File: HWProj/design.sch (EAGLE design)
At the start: 72 parts, among them IC1 LM311N, IC10 TL071P, IC11 TL071P, IC12 TL071P, IC13 TL071P, IC14 TL071P, IC15 TL071P, IC16 LM311N, IC17 TL071P, IC18 TL071P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

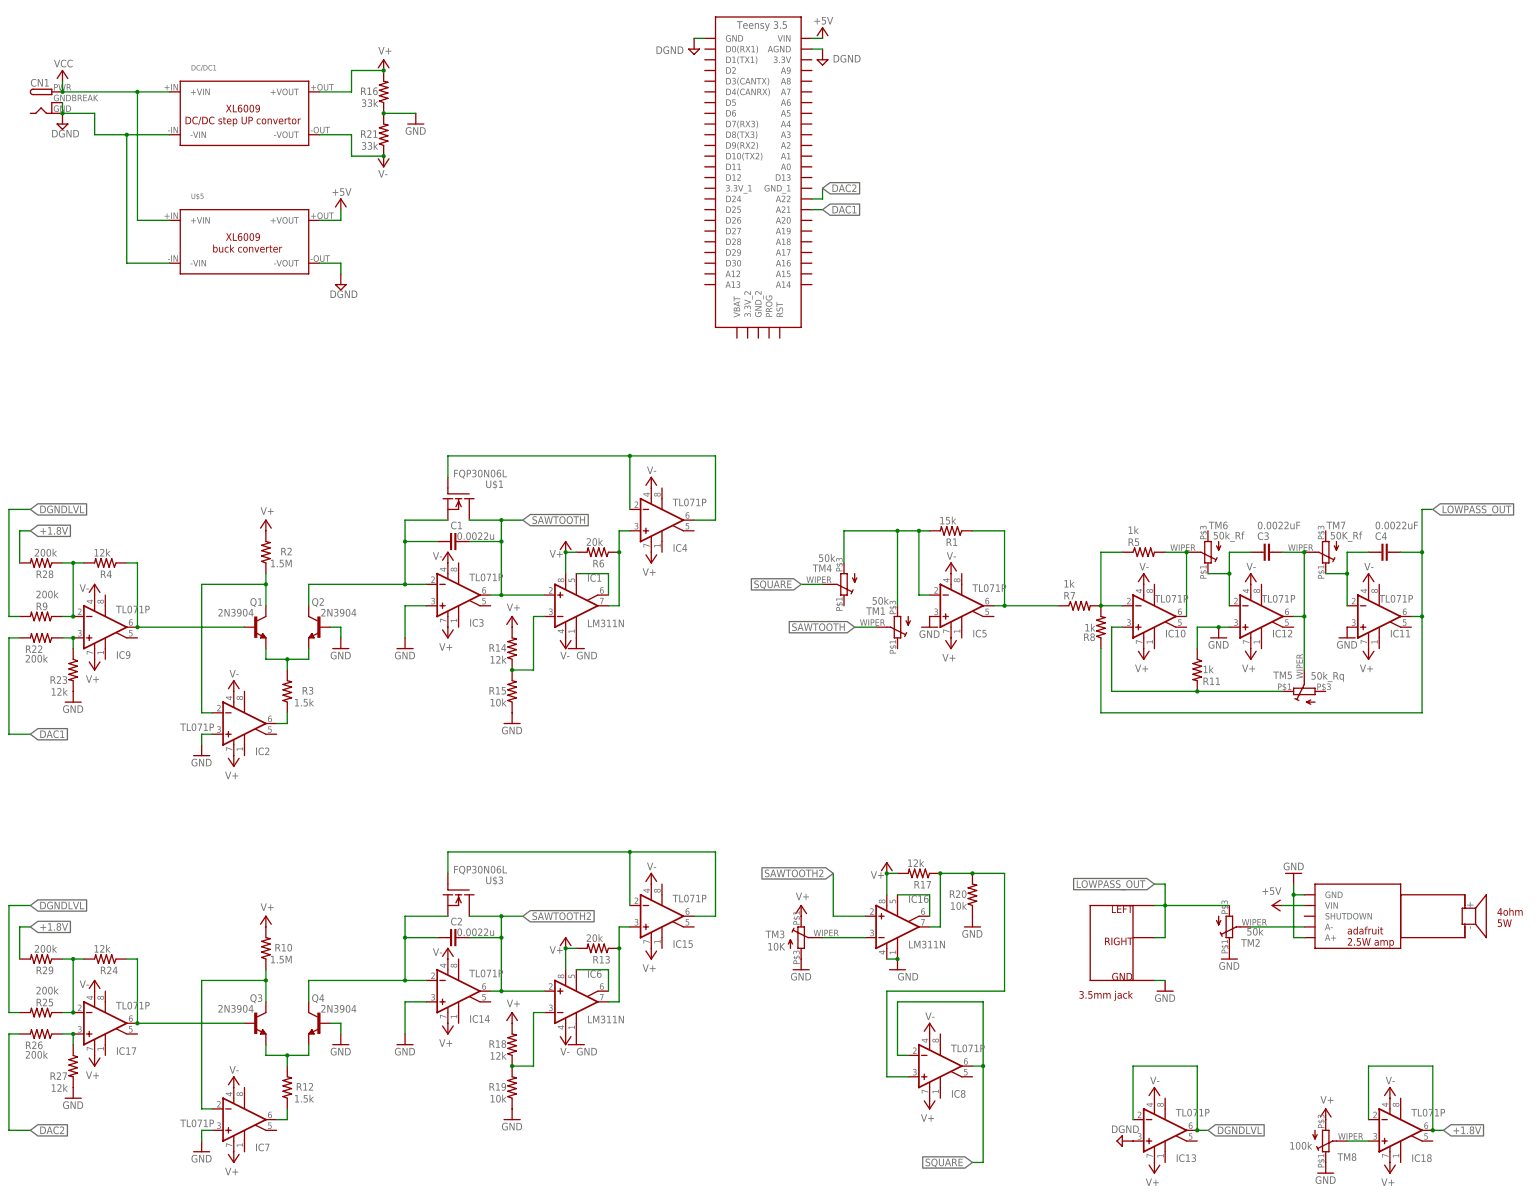
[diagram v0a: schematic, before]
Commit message: fixed ground ref for amp, replaced boost converter
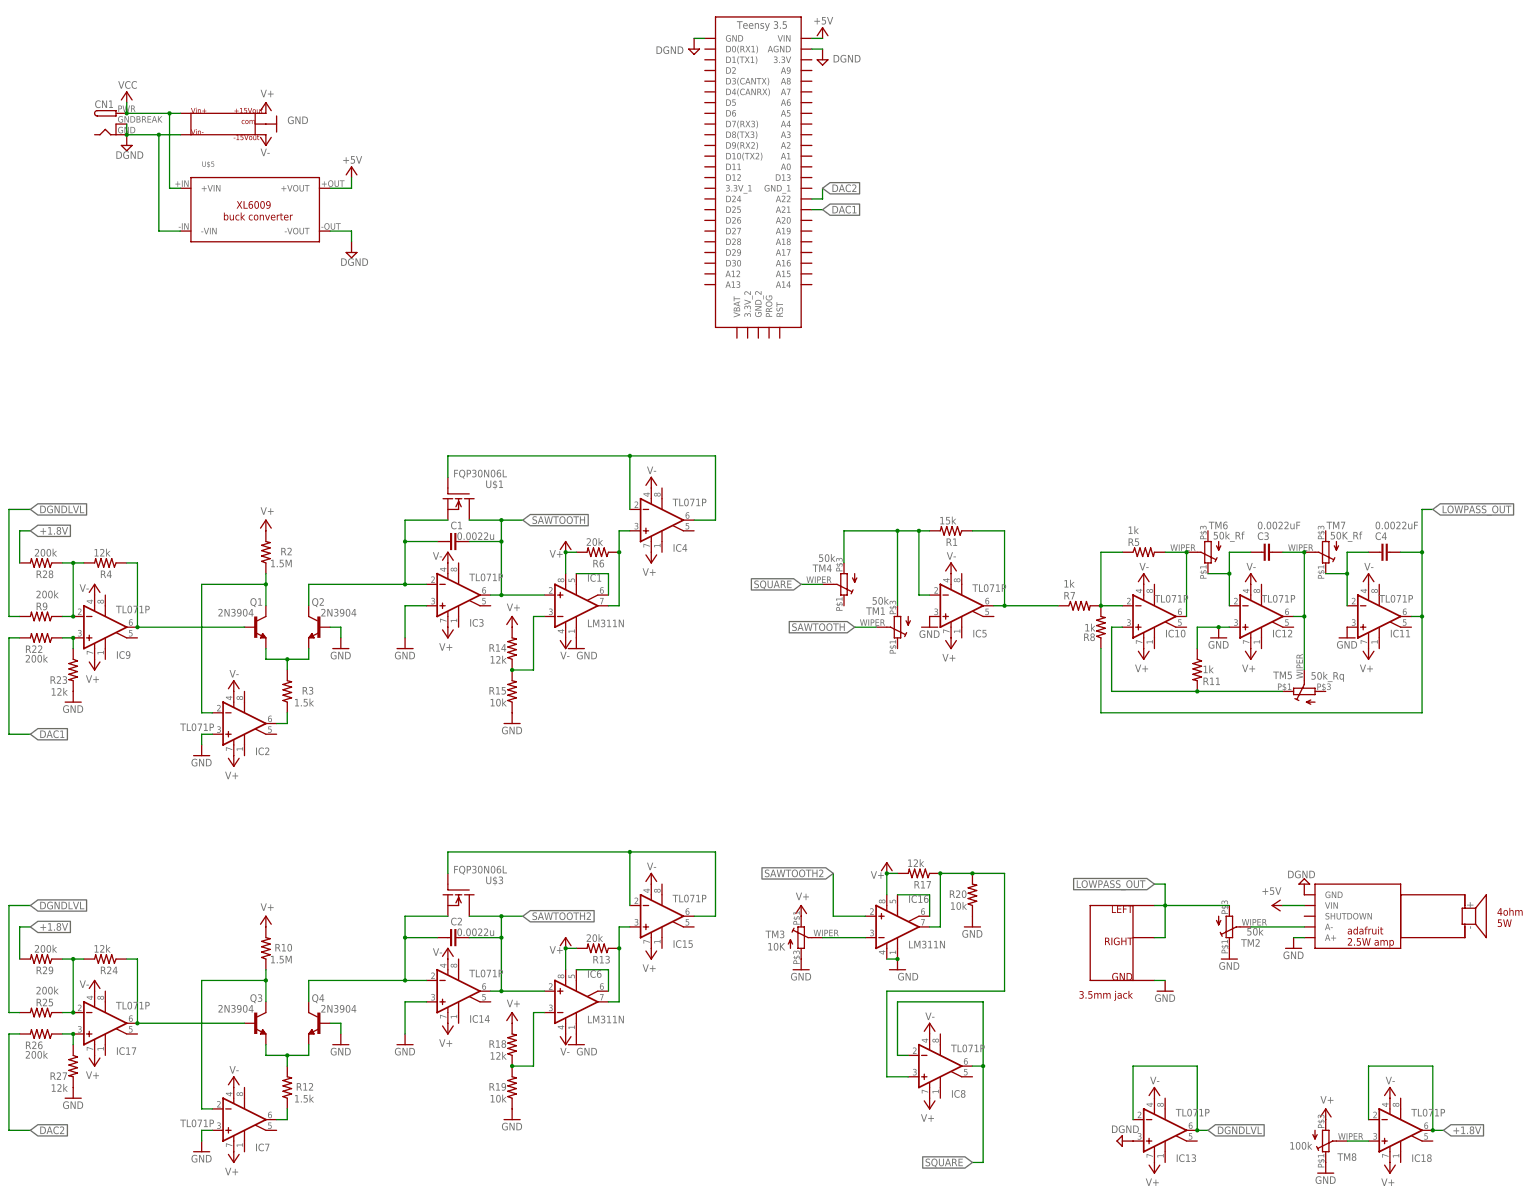
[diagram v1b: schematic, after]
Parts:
- removed DC/DC1: DC/DC-STEP-UP-XL6009, userlib:DC/DC-STEP-UP-XL6009
- removed R16, R21: 33k, HyTechDevices:RESISTORAXIAL-0.3
- added U$7: +/-15V_BOOST_CONVERTER, userlib:+/-15V_BOOST_CONVERTER
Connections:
- net DGND: now also U$2.GND, U$7.1; no longer DC/DC1.-VIN
- net GND: now also U$7.7; no longer R16.1, R21.2, U$2.GND
- net V+: now also U$7.6; no longer DC/DC1.+VOUT, R16.2
- net V-: now also U$7.8; no longer DC/DC1.-VOUT, R21.1
- net VCC: now also U$7.2; no longer DC/DC1.+VIN
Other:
- note added: "needs testing!!"
- note removed: "+/-15V"
- moved on the sheet: CN1, U$5

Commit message: added board rev0
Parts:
- C1, C2: device HyTechDevices:CAPCAP_WIMA -> HyTechDevices:CAPPTH1
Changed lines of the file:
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@@
 <layers>
 <layer number="1" name="Top" color="4" fill="1" visible="yes" active="no"/>
-<layer number="2" name="Route2" color="1" fill="3" visible="yes" active="no"/>
-<layer number="3" name="Route3" color="4" fill="3" visible="yes" active="no"/>
-<layer number="4" name="Route4" color="1" fill="4" visible="yes" active="no"/>
-<layer number="5" name="Route5" color="4" fill="4" visible="yes" active="no"/>
-<layer number="6" name="Route6" color="1" fill="8" visible="yes" active="no"/>
-<layer number="7" name="Route7" color="4" fill="8" visible="yes" active="no"/>
-<layer number="8" name="Route8" color="1" fill="2" visible="yes" active="no"/>
-<layer number="9" name="Route9" color="4" fill="2" visible="yes" active="no"/>
-<layer number="10" name="Route10" color="1" fill="7" visible="yes" active="no"/>
-<layer number="11" name="Route11" color="4" fill="7" visible="yes" active="no"/>
-<layer number="12" name="Route12" color="1" fill="5" visible="yes" active="no"/>
-<layer number="13" name="Route13" color="4" fill="5" visible="yes" active="no"/>
-<layer number="14" name="Route14" color="1" fill="6" visible="yes" active="no"/>
-<layer number="15" name="Route15" color="4" fill="6" visible="yes" active="no"/>
+<layer number="2" name="Route2" color="16" fill="1" visible="yes" active="no"/>
+<layer number="3" name="Route3" color="17" fill="1" visible="yes" active="no"/>
+<layer number="4" name="Route4" color="18" fill="1" visible="yes" active="no"/>
+<layer number="5" name="Route5" color="19" fill="1" visible="yes" active="no"/>
+<layer number="6" name="Route6" color="25" fill="1" visible="yes" active="no"/>
+<layer number="7" name="Route7" color="26" fill="1" visible="yes" active="no"/>
+<layer number="8" name="Route8" color="27" fill="1" visible="yes" active="no"/>
+<layer number="9" name="Route9" color="28" fill="1" visible="yes" active="no"/>
+<layer number="10" name="Route10" color="29" fill="1" visible="yes" active="no"/>
+<layer number="11" name="Route11" color="30" fill="1" visible="yes" active="no"/>
+<layer number="12" name="Route12" color="20" fill="1" visible="yes" active="no"/>
+<layer number="13" name="Route13" color="21" fill="1" visible="yes" active="no"/>
+<layer number="14" name="Route14" color="22" fill="1" visible="yes" active="no"/>
+<layer number="15" name="Route15" color="23" fill="1" visible="yes" active="no"/>
 <layer number="16" name="Bottom" color="1" fill="1" visible="yes" active="no"/>
 <layer number="17" name="Pads" color="2" fill="1" visible="yes" active="no"/>
 <layer number="18" name="Vias" color="2" fill="1" visible="yes" active="no"/>
 <layer number="19" name="Unrouted" color="6" fill="1" visible="yes" active="no"/>
-<layer number="20" name="Dimension" color="15" fill="1" visible="yes" active="no"/>
+<layer number="20" name="Dimension" color="24" fill="1" visible="yes" active="no"/>
 <layer number="21" name="tPlace" color="7" fill="1" visible="yes" active="no"/>
 <layer number="22" name="bPlace" color="7" fill="1" visible="yes" active="no"/>
@@
 <part name="SUPPLY2" library="supply2" library_urn="urn:adsk.eagle:library:372" deviceset="V+" device=""/>
 <part name="GND3" library="HyTechSymbols" deviceset="GND" device=""/>
-<part name="C1" library="HyTechDevices" deviceset="CAP" device="CAP_WIMA" value="0.0022u"/>
+<part name="C1" library="HyTechDevices" deviceset="CAP" device="PTH1" value="0.0022u"/>
 <part name="GND4" library="HyTechSymbols" deviceset="GND" device=""/>
 <part name="SUPPLY3" library="supply2" library_urn="urn:adsk.eagle:library:372" deviceset="V-" device=""/>
@@
 <part name="SUPPLY15" library="supply2" library_urn="urn:adsk.eagle:library:372" deviceset="V+" device=""/>
 <part name="GND11" library="HyTechSymbols" deviceset="GND" device=""/>
-<part name="C2" library="HyTechDevices" deviceset="CAP" device="CAP_WIMA" value="0.0022u"/>
+<part name="C2" library="HyTechDevices" deviceset="CAP" device="PTH1" value="0.0022u"/>
 <part name="GND14" library="HyTechSymbols" deviceset="GND" device=""/>
 <part name="SUPPLY29" library="supply2" library_urn="urn:adsk.eagle:library:372" deviceset="V-" device=""/>
@@
 <part name="U$6" library="userlib" deviceset="3.5MM_AUDIO_JACK" device=""/>
 <part name="SUPPLY39" library="supply2" library_urn="urn:adsk.eagle:library:372" deviceset="DGND" device=""/>
-<part name="U$7" library="userlib" deviceset="+/-15V_BOOST_CONVERTER" device=""/>
 <part name="SUPPLY40" library="supply2" library_urn="urn:adsk.eagle:library:372" deviceset="V+" device=""/>
 <part name="SUPPLY49" library="supply2" library_urn="urn:adsk.eagle:library:372" deviceset="V-" device=""/>
 <part name="GND5" library="HyTechSymbols" deviceset="GND" device=""/>
+<part name="U$7" library="userlib" deviceset="+/-15V_BOOST_CONVERTER" device=""/>
 </parts>
 <sheets>
@@
 <attribute name="VALUE" x="325.247" y="86.995" size="1.778" layer="96" rot="R180"/>
 </instance>
-<instance part="U$7" gate="G$1" x="66.04" y="264.16" smashed="yes"/>
 <instance part="SUPPLY40" gate="1" x="76.2" y="269.24" smashed="yes">
 <attribute name="VALUE" x="74.93" y="270.51" size="1.778" layer="96"/>
@@
 <attribute name="VALUE" x="81.28" y="264.16" size="1.778" layer="96"/>
 </instance>
+<instance part="U$7" gate="G$1" x="66.04" y="264.16" smashed="yes"/>
 </instances>
 <busses>
@@
 </segment>
 <segment>
+<pinref part="SUPPLY40" gate="1" pin="V+"/>
 <pinref part="U$7" gate="G$1" pin="6"/>
-<pinref part="SUPPLY40" gate="1" pin="V+"/>
 </segment>
 </net>
@@
 </segment>
 <segment>
+<pinref part="GND5" gate="1" pin="GND"/>
 <pinref part="U$7" gate="G$1" pin="7"/>
-<pinref part="GND5" gate="1" pin="GND"/>
 </segment>
 </net>
@@
 </segment>
 <segment>
+<pinref part="SUPPLY49" gate="1" pin="V-"/>
 <pinref part="U$7" gate="G$1" pin="8"/>
-<pinref part="SUPPLY49" gate="1" pin="V-"/>
 </segment>
 </net>
@@
 <wire x1="43.18" y1="264.16" x2="43.18" y2="261.62" width="0.1524" layer="91"/>
 <junction x="43.18" y="261.62"/>
-<pinref part="U$7" gate="G$1" pin="1"/>
 <wire x1="43.18" y1="261.62" x2="50.8" y2="261.62" width="0.1524" layer="91"/>
 <pinref part="U$5" gate="G$1" pin="-VIN"/>
@@
 <wire x1="50.8" y1="238.76" x2="50.8" y2="261.62" width="0.1524" layer="91"/>
 <junction x="50.8" y="261.62"/>
+<pinref part="U$7" gate="G$1" pin="1"/>
 </segment>
 <segment>
@@
 <junction x="43.18" y="266.7"/>
 <wire x1="55.88" y1="266.7" x2="53.34" y2="266.7" width="0.1524" layer="91"/>
-<pinref part="U$7" gate="G$1" pin="2"/>
 <pinref part="U$5" gate="G$1" pin="+VIN"/>
 <wire x1="53.34" y1="266.7" x2="43.18" y2="266.7" width="0.1524" layer="91"/>
@@
 <wire x1="53.34" y1="248.92" x2="53.34" y2="266.7" width="0.1524" layer="91"/>
 <junction x="53.34" y="266.7"/>
-</segment>
-</net>
+<pinref part="U$7" gate="G$1" pin="2"/>
+</segment>
+</net>

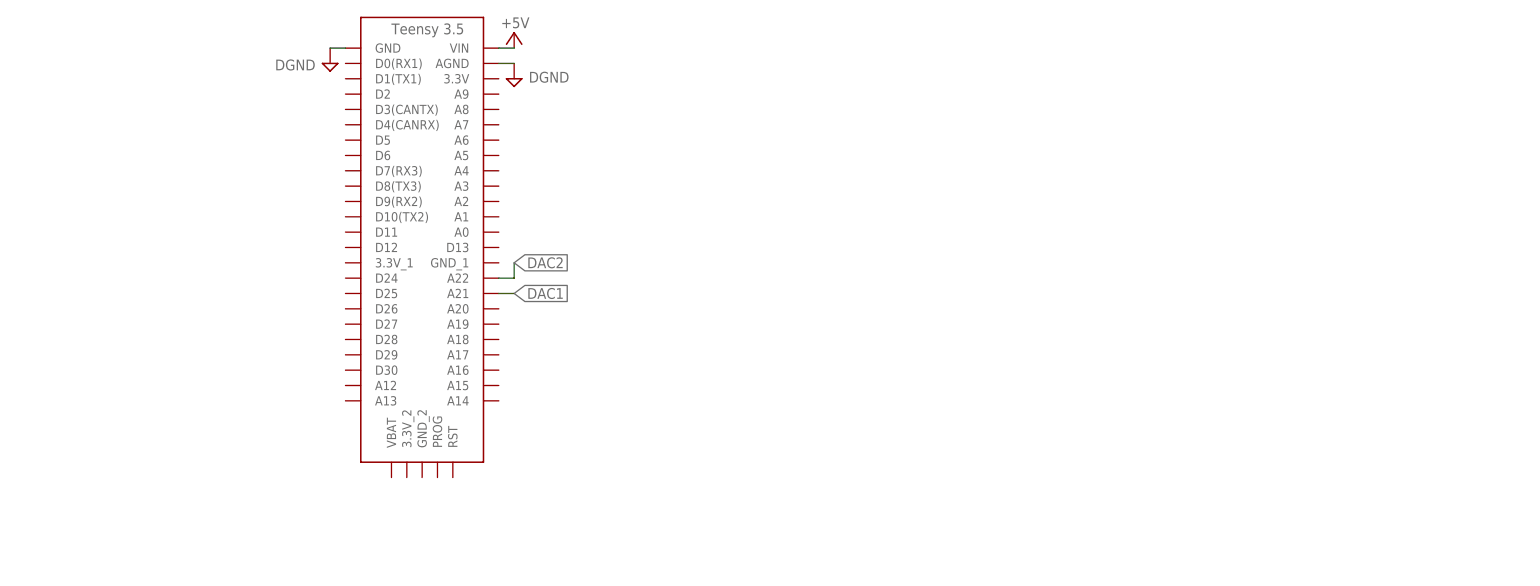
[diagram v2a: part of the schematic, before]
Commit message: added motor, sensors, and servos--board rev1
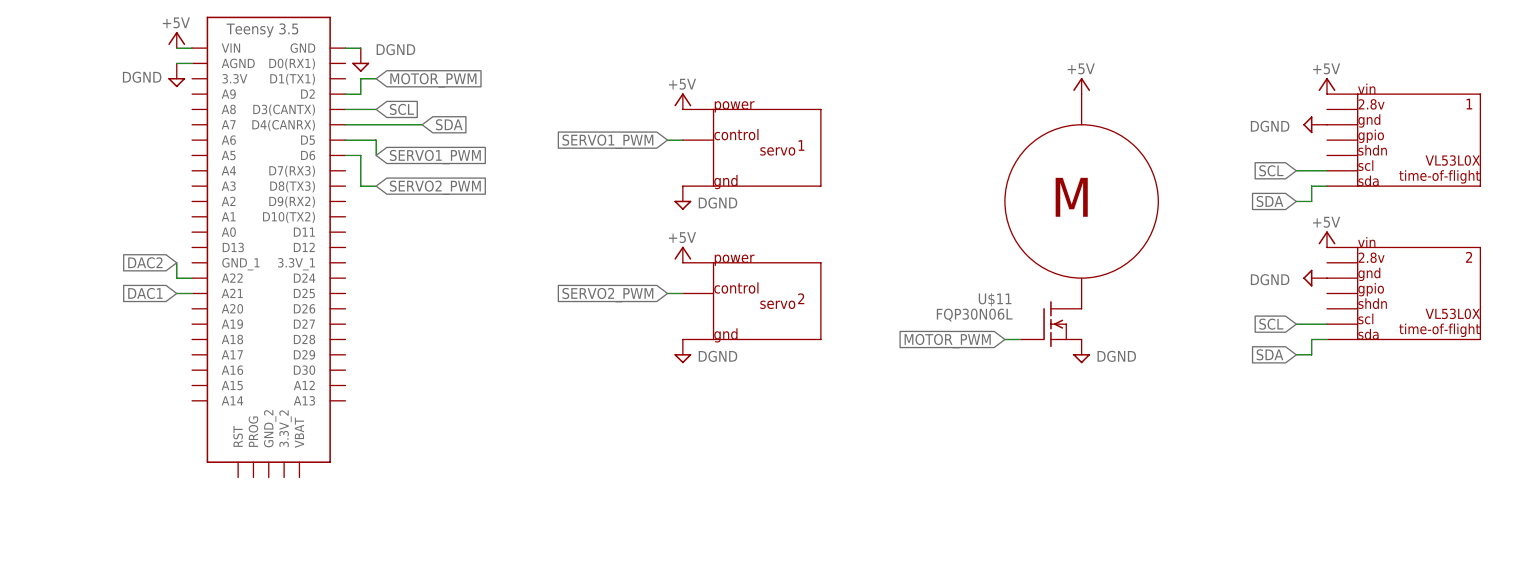
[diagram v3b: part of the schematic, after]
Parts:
- added U$10: 3872_MOTOR, HyTechDevices:3872_MOTOR
- added U$11: FQP30N06L, HyTechDevices:FQP30N06L
- added U$12, U$13: VL53L0X, HyTechDevices:VL53L0X
- added U$8, U$9: SERVO_3PIN_HEADER, HyTechDevices:SERVO_3PIN_HEADER
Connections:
- new net MOTOR_PWM: U$11.G, U$4.D2
- new net N$33: U$10.-, U$11.D
- new net SCL: U$12.SCL, U$13.SCL, U$4.D3(CANTX)
- new net SDA: U$12.SDA, U$13.SDA, U$4.D4(CANRX)
- new net SERVO1_PWM: U$4.D5, U$8.CONTROL
- new net SERVO2_PWM: U$4.D6, U$9.CONTROL
- net +5V: now also U$10.+, U$12.VIN, U$13.VIN, U$8.POWER, U$9.POWER
- net DGND: now also U$11.S, U$12.GND, U$13.GND, U$8.GND, U$9.GND
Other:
- note added: "1"
- note added: "2"
